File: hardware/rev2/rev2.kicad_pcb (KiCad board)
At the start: 4 copper layers, 60 x 40 mm, 80 parts, among them J7 USB_C_Receptacle_USB2.0_16P, SW1 SW_Push, U1 ESP32-S3FN8, U2 SX1262IMLTRT

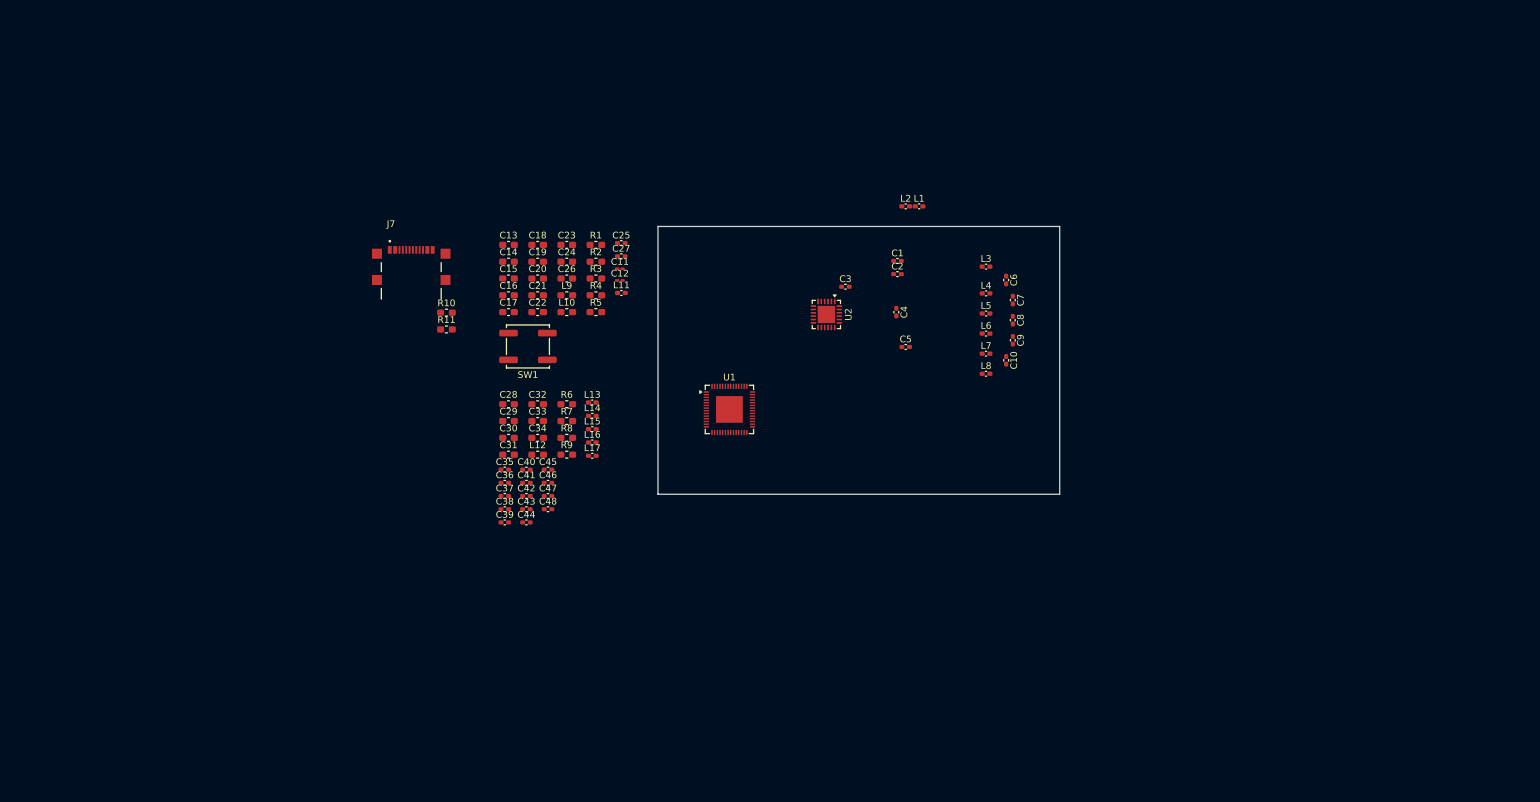
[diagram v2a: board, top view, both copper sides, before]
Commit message: added all footprints for esp32 and sx1262, began layouting
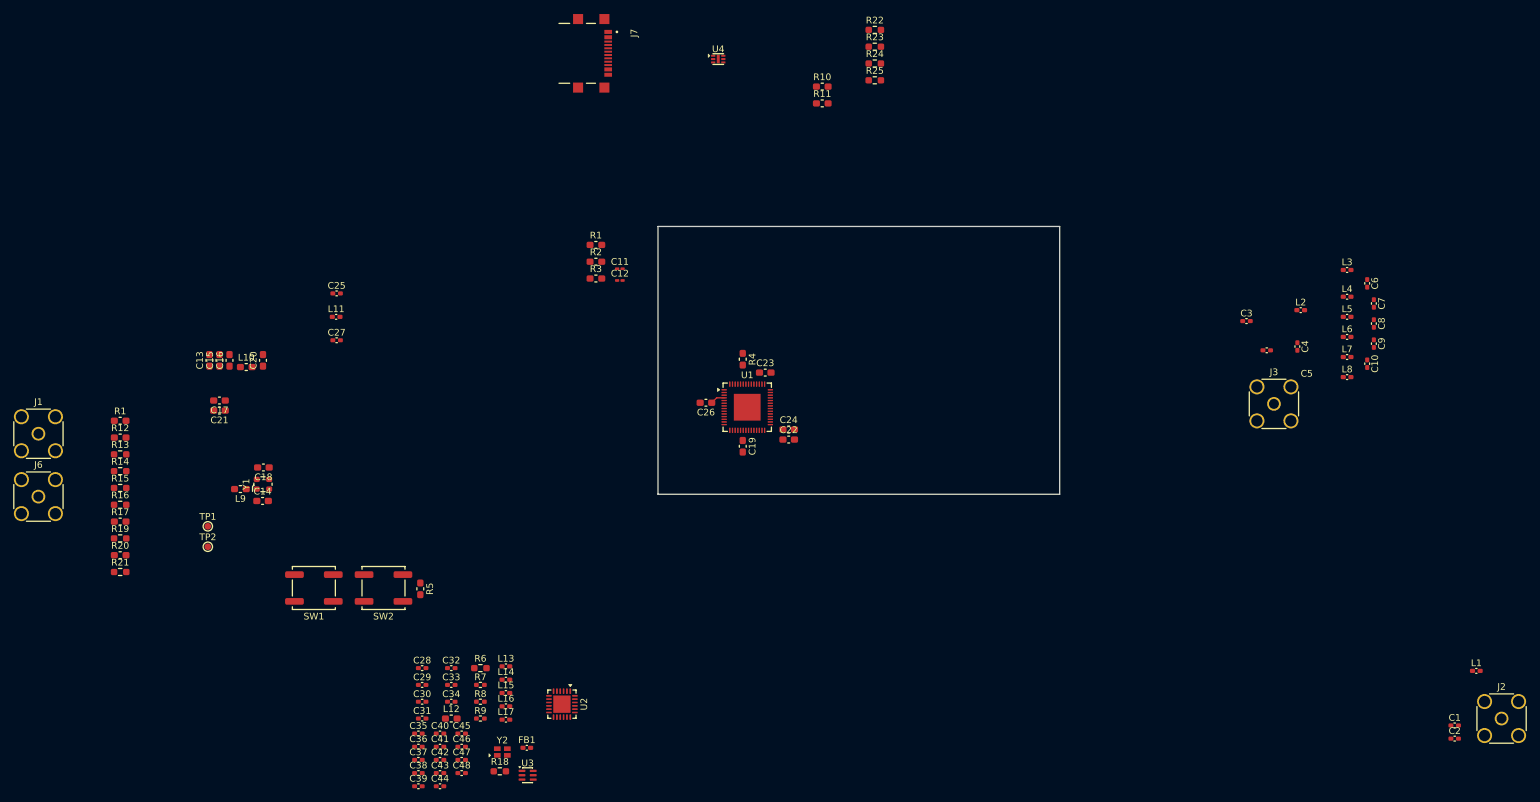
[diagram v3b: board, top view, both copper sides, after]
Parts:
- added FB1: FerriteBead_Small, Inductor_SMD:L_0402_1005Metric_Pad0.77x0.64mm_HandSolder, F.Cu at (108.4, 134.9)
- added J1: SMA, Connector_Coaxial:SMA_Amphenol_132134-16_Vertical, F.Cu at (35.5, 88.0)
- added J2: SMA, Connector_Coaxial:SMA_Amphenol_132134-16_Vertical, F.Cu at (254.0, 130.5)
- added J3: SMA, Connector_Coaxial:SMA_Amphenol_132134-16_Vertical, F.Cu at (220.0, 83.5)
- added J6: SMA, Connector_Coaxial:SMA_Amphenol_132134-16_Vertical, F.Cu at (35.5, 97.3)
- added R1: 10k, Inductor_SMD:L_0603_1608Metric_Pad1.05x0.95mm_HandSolder, F.Cu at (47.7, 86.0)
- added R12: 499 R, Inductor_SMD:L_0603_1608Metric_Pad1.05x0.95mm_HandSolder, F.Cu at (47.7, 88.5)
- added R13: 0R, Resistor_SMD:R_0603_1608Metric_Pad0.98x0.95mm_HandSolder, F.Cu at (47.7, 91.0)
- added R14: 0R, Resistor_SMD:R_0603_1608Metric_Pad0.98x0.95mm_HandSolder, F.Cu at (47.7, 93.5)
- added R15: 0R, Resistor_SMD:R_0603_1608Metric_Pad0.98x0.95mm_HandSolder, F.Cu at (47.7, 96.1)
- added R16: 0R, Resistor_SMD:R_0603_1608Metric_Pad0.98x0.95mm_HandSolder, F.Cu at (47.7, 98.6)
- added R17: 10k, Inductor_SMD:L_0603_1608Metric_Pad1.05x0.95mm_HandSolder, F.Cu at (47.7, 101.1)
- added R18: 10k, Resistor_SMD:R_0603_1608Metric_Pad0.98x0.95mm_HandSolder, F.Cu at (104.4, 138.4)
- added R19: 0R, Resistor_SMD:R_0603_1608Metric_Pad0.98x0.95mm_HandSolder, F.Cu at (47.7, 103.6)
- added R20: 499 R, Inductor_SMD:L_0603_1608Metric_Pad1.05x0.95mm_HandSolder, F.Cu at (47.7, 106.1)
- added R21: 0R, Resistor_SMD:R_0603_1608Metric_Pad0.98x0.95mm_HandSolder, F.Cu at (47.7, 108.6)
- added R22: 0R, Resistor_SMD:R_0603_1608Metric_Pad0.98x0.95mm_HandSolder, F.Cu at (160.4, 27.6)
- added R23: 0R, Resistor_SMD:R_0603_1608Metric_Pad0.98x0.95mm_HandSolder, F.Cu at (160.4, 30.1)
- added R24: 0R, Resistor_SMD:R_0603_1608Metric_Pad0.98x0.95mm_HandSolder, F.Cu at (160.4, 32.7)
- added R25: 0R, Resistor_SMD:R_0603_1608Metric_Pad0.98x0.95mm_HandSolder, F.Cu at (160.4, 35.2)
- added SW2: SW_Push, Button_Switch_SMD:SW_Push_1P1T_NO_CK_KSC7xxJ, F.Cu at (87.0, 111.0)
- added TP1: TestPoint, TestPoint:TestPoint_Pad_D1.0mm, F.Cu at (60.8, 101.8)
- added TP2: TestPoint, TestPoint:TestPoint_Pad_D1.0mm, F.Cu at (60.8, 104.8)
- added U3: PE4259, Package_TO_SOT_SMD:SOT-363_SC-70-6, F.Cu at (108.5, 139.0)
- added U4: EClamp2522P, _footprints:SLP1616P6, F.Cu at (137.0, 32.0)
- added Y1: ECS-2520SMV-400-FN-TR, Oscillator:Oscillator_SMD_ECS_2520MV-xxx-xx-4Pin_2.5x2.0mm, F.Cu at (69.0, 95.5)
- added Y2: TXO-20CSMV-320, _footprints:TXO-20CSMV-320, F.Cu at (104.8, 135.5)
- C28, C32: value 100n -> 0.1 uF; footprint Capacitor_SMD:C_0603_1608Metric_Pad1.08x0.95mm_HandSolder -> Capacitor_SMD:C_0402_1005Metric_Pad0.74x0.62mm_HandSolder
- C29, C33: footprint Capacitor_SMD:C_0603_1608Metric_Pad1.08x0.95mm_HandSolder -> Capacitor_SMD:C_0402_1005Metric_Pad0.74x0.62mm_HandSolder
- C30: value 10p -> 10 pF; footprint Capacitor_SMD:C_0603_1608Metric_Pad1.08x0.95mm_HandSolder -> Capacitor_SMD:C_0402_1005Metric_Pad0.74x0.62mm_HandSolder
- C31: value 100n -> 1 uF; footprint Capacitor_SMD:C_0603_1608Metric_Pad1.08x0.95mm_HandSolder -> Capacitor_SMD:C_0402_1005Metric_Pad0.74x0.62mm_HandSolder
- C34: value 470n -> 0.47 uF; footprint Capacitor_SMD:C_0603_1608Metric_Pad1.08x0.95mm_HandSolder -> Capacitor_SMD:C_0402_1005Metric_Pad0.74x0.62mm_HandSolder
- C35, C42, C46: value DC Block -> C
- C37: value 47p -> 47 pF
- C38: value 47n -> 47 nF
- C44, C45: value 1n -> 1 nF
- L12: value 15u -> 15 uH
- L14: value 115n -> L
- L9: value TBD (24 nH) -> 24 nH (Test)
- R4, R5: value 10K -> 10k
- R6: value pull-up -> 10k; footprint Inductor_SMD:L_0603_1608Metric_Pad1.05x0.95mm_HandSolder -> Resistor_SMD:R_0603_1608Metric_Pad0.98x0.95mm_HandSolder
- R7: value 220R -> 0 R; footprint Inductor_SMD:L_0603_1608Metric_Pad1.05x0.95mm_HandSolder -> Resistor_SMD:R_0402_1005Metric_Pad0.72x0.64mm_HandSolder
- R8, R9: value 100R -> 100 R; footprint Inductor_SMD:L_0603_1608Metric_Pad1.05x0.95mm_HandSolder -> Resistor_SMD:R_0402_1005Metric_Pad0.72x0.64mm_HandSolder
- moved C1 108.4 mm to (247.0, 131.5)
- moved C2 108.4 mm to (247.0, 133.5)
- moved L1 108.4 mm to (250.2, 123.4)
- moved U2 70.3 mm to (113.7, 128.3)
- moved R10 65.5 mm to (152.5, 36.1)
- moved R11 65.5 mm to (152.5, 38.6)
- moved L2 61.0 mm to (224.0, 69.5)
- moved C3 60.1 mm to (215.9, 71.1)
- moved C4 60.1 mm to (223.5, 74.9)
- moved L9 56.7 mm to (65.6, 96.2), turned to 180 degrees
- moved C10 53.9 mm to (233.9, 77.5)
- moved C5 53.9 mm to (218.9, 75.5)
- moved C6 53.9 mm to (233.9, 65.5)
- moved C7 53.9 mm to (234.9, 68.5)
- moved C8 53.9 mm to (234.9, 71.5)
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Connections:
- net Net-(J6-In) renamed /ESP32/LNA_IN
- net Net-(U1-GPIO45) renamed /ESP32/GPIO45
- C30 pad 2: Net-(U2-XTA) -> Net-(Y2-Output)
- J7 pad A6: /USB_D+ -> Net-(J7-D+-PadA6)
- J7 pad A7: /USB_D- -> Net-(J7-D--PadA7)
- J7 pad B6: /USB_D+ -> Net-(J7-D+-PadA6)
- J7 pad B7: /USB_D- -> Net-(J7-D--PadA7)
- L4 pad 1: /RXD/SDA? -> /RXD/SDA
- L5 pad 1: /TXD/SCL? -> /TXD/SCL
- R7 pad 1: Net-(Y2-OUT) -> Net-(U2-XTA)
- R8 pad 1: /SX1262/RX_EN -> /ESP32/RX_EN
- SW1 pad 2: Net-(U1-GPIO0) -> /ESP32/GPIO0
- U1 pad 10: unconnected-(U1-GPIO5-Pad10) -> /EXTINT
- U1 pad 11: unconnected-(U1-GPIO6-Pad11) -> /SX1262/Reset
- U1 pad 12: /ESP32/MISO -> /ESP32/DIO1
- U1 pad 13: /ESP32/MOSI -> /ESP32/BUSY
- U1 pad 14: /ESP32/CS -> /ESP32/RX_EN
- U1 pad 15: /ESP32/SCK -> /ESP32/SPI_CS
- U1 pad 16: /SX1262/Reset -> /ESP32/SPI_MOSI
- U1 pad 17: /ESP32/DIO1 -> /ESP32/SPI_CLK
- U1 pad 18: /ESP32/BUSY -> /ESP32/SPI_MISO
- U1 pad 23: unconnected-(U1-GPIO17-Pad23) -> /ESP32/U1TXD/SCL
- U1 pad 24: unconnected-(U1-GPIO18-Pad24) -> /ESP32/U1RXD/SDA
- U1 pad 49: unconnected-(U1-U0TXD-Pad49) -> /ESP32/U0TXD
- U1 pad 5: Net-(U1-GPIO0) -> /ESP32/GPIO0
- U1 pad 50: unconnected-(U1-U0RXD-Pad50) -> /ESP32/U0RXD
- U1 pad 52: unconnected-(U1-GPIO46-Pad52) -> /ESP32/GPIO46
- U1 pad 9: unconnected-(U1-GPIO4-Pad9) -> /RESET_N
- U2 pad 18: /ESP32/SCK -> /ESP32/CLK
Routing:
- net Net-(U1-CHIP_PU): track 0.00 -> 2.16 mm

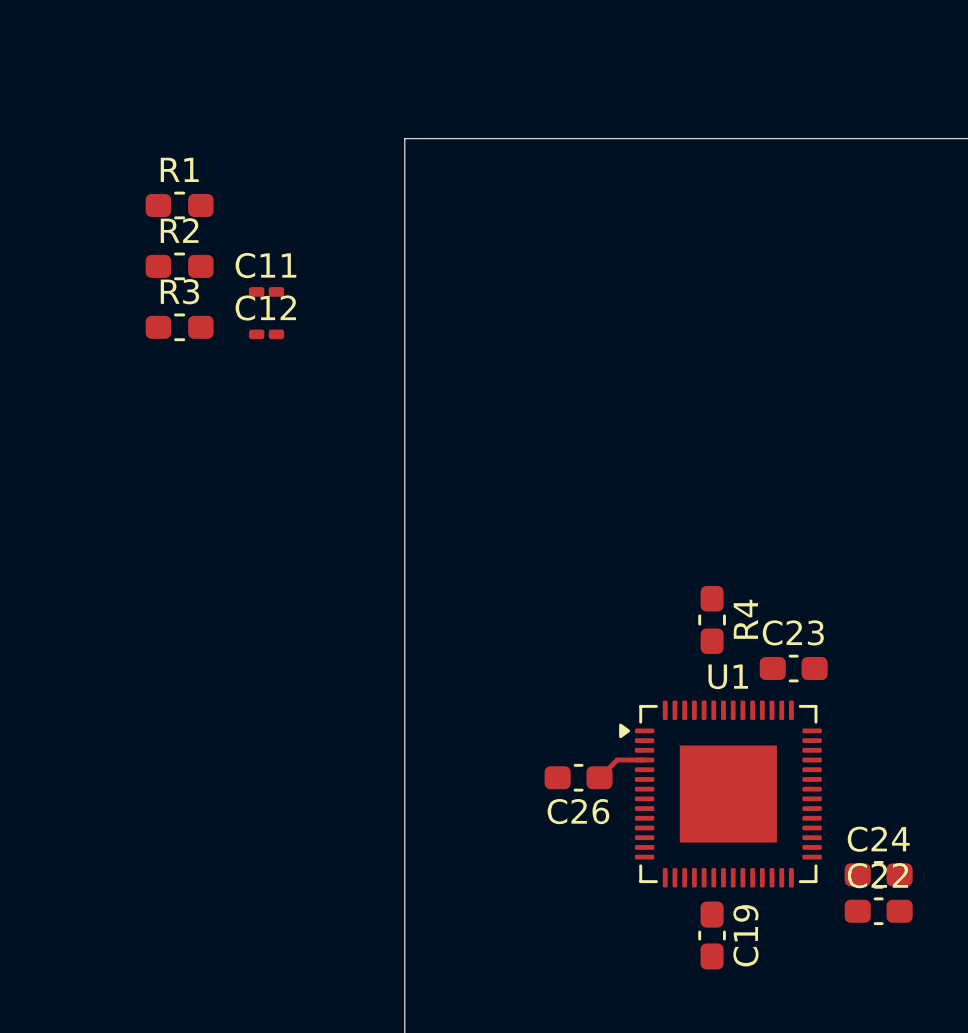
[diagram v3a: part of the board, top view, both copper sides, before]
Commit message: added rules for impedance
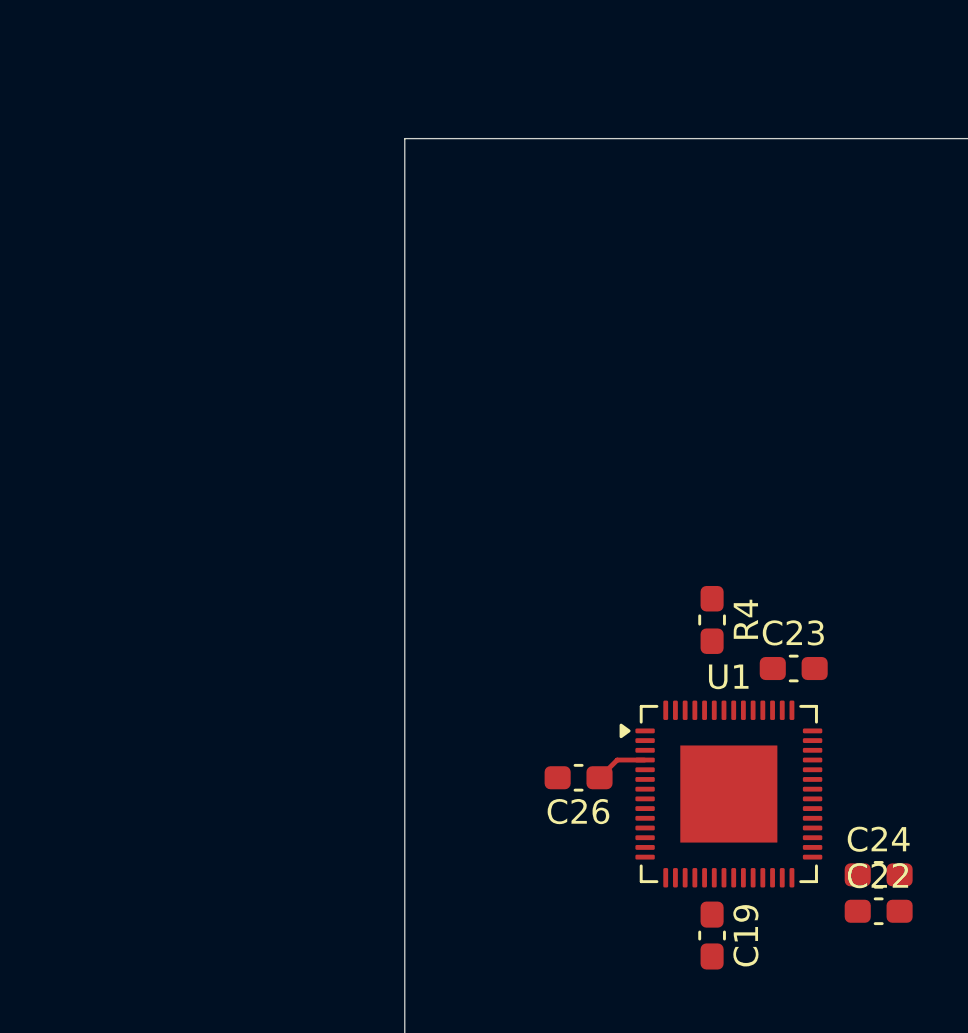
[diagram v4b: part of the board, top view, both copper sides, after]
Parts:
- removed C11, C12: NC, Capacitor_SMD:C_0201_0603Metric_Pad0.64x0.40mm_HandSolder
- removed the R1 at (118.7, 59.8)
- removed R2, R3: 22R, Inductor_SMD:L_0603_1608Metric_Pad1.05x0.95mm_HandSolder

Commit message: continued routing and layouting
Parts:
- removed R24, R25: 0R, Resistor_SMD:R_0603_1608Metric_Pad0.98x0.95mm_HandSolder
- added AE1: Antenna_Chip, _footprints:ACAG0301-2450-T, F.Cu at (130.9, 59.5)
- J1: renamed from J7; moved to B.Cu
- R1: renamed from R10; moved to B.Cu
- R2: renamed from R11; moved to B.Cu
- moved J2 152.6 mm to (128.4, 44.0)
- moved C2 133.3 mm to (135.7, 60.1), turned to -90 degrees
- moved L1 129.7 mm to (137.3, 59.5)
- moved C1 129.6 mm to (138.9, 60.1), turned to -90 degrees
- moved J7 111.3 mm to (137.7, 43.8)
- moved C46 106.0 mm to (184.3, 76.3), turned to 90 degrees
- moved C42 104.3 mm to (176.6, 75.1), turned to 180 degrees
- moved C45 102.0 mm to (180.8, 76.3), turned to 90 degrees
- moved C41 101.2 mm to (174.3, 75.3), turned to -90 degrees
- moved C44 99.1 mm to (179.1, 76.8)
- moved C36 98.9 mm to (165.7, 72.3)
- moved R21 97.3 mm to (176.3, 72.8), turned to 180 degrees
- moved C35 97.0 mm to (165.7, 73.3)
- moved C40 96.5 mm to (170.3, 75.8)
- moved C43 94.9 mm to (176.6, 78.6), turned to 180 degrees
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- renumbered C13 to C11, C17 to C12, C14 to C13, C15 to C14, C21 to C15, C18 to C17, C19 to C18, C20 to C19, C22 to C20, C23 to C21, C24 to C22, C26 to C23, C25 to C24, C27 to C25, C28 to C26, C30 to C27, C29 to C28, C31 to C29, C32 to C30, C33 to C31, C34 to C32, C35 to C33, C36 to C34, C37 to C35, C38 to C36, C39 to C37, C40 to C38, C41 to C39, C42 to C40, C43 to C41, C44 to C42, C45 to C43, C46 to C44, C47 to C45, C48 to C46, J1 to J7, R14 to R10, R15 to R11, R16 to R12, R12 to R13, R19 to R14, R20 to R15, R21 to R16, R6 to R17, R7 to R18, R8 to R19, R9 to R20, R18 to R21, R22 to R3, R23 to R4, R4 to R6, R17 to R7, R1 to R8, R13 to R9, SW2 to SW1, SW1 to SW2, U4 to U1, U1 to U2, U2 to U3, U3 to U4
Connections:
- net Net-(J7-D+-PadA6) renamed /D+
- net Net-(J7-D--PadA7) renamed /D-
- net Net-(U4-DM_In) renamed /D+*
- net Net-(U4-DP_In) renamed /D-*
- U1 pad 4: Net-(U4-DP_Out) -> /USB_D-
- U1 pad 5: Net-(U4-DM_Out) -> /USB_D+
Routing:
- net /Antenna_WiFi: track 0.00 -> 7.49 mm
- net /D+: track 0.00 -> 5.97 mm, vias 0 -> 1
- net /D-: track 0.00 -> 5.13 mm, vias 0 -> 1
- net +5V: track 0.00 -> 4.63 mm, vias 0 -> 7
- net Net-(AE1-FEED): track 0.00 -> 4.23 mm
- net /ESP32/LNA_IN: track 0.00 -> 3.70 mm
- net Net-(J1-CC2): track 0.00 -> 2.67 mm
- net Net-(J1-CC1): track 0.00 -> 2.67 mm
- net /USB_D-: track 0.00 -> 1.67 mm
- net /USB_D+: track 0.00 -> 1.67 mm
- net /ESP32/GPIO0: track 0.00 -> 1.64 mm, vias 0 -> 1
- net +3V3: track 0.00 -> 0.65 mm, vias 0 -> 4
- net Net-(U2-CHIP_PU): vias 0 -> 1
- added copper zone on F.Cu, net +3V3
- added copper zone on B.Cu, net +5V
- added copper zone on In2.Cu, net +5V
- added copper zone on B.Cu, net /ESP32/LNA_IN
- added copper zone on B.Cu, net GND
- added copper zone on F.Cu, net GND
- added copper zone on F.Cu, net Net-(C19-Pad1)
